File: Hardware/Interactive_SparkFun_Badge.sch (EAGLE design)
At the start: 31 parts, among them J1 AVR_SPI_PRG_6NS, U1 ATMEGA328P, Y1 8MHZ

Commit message: New board design
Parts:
- removed STANDOFF1: STAND-OFF, SparkFun-Electromechanical:STAND-OFF
- removed U$2: FLAME, Local Library:FLAME
- LOGO1: value OSHW-LOGOM -> OSHW-LOGOL; device SparkFun-Aesthetics:OSHW-LOGOM -> SparkFun-Aesthetics:OSHW-LOGOL
- LOGO2: value SFE_LOGO_NAME.1_INCH -> SFE_LOGO_NAME_FLAME.3_INCH; device SparkFun-Aesthetics:SFE_LOGO_NAME.1_INCH -> SparkFun-Aesthetics:SFE_LOGO_NAME_FLAME.3_INCH
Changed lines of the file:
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@@
 <grid distance="0.1" unitdist="inch" unit="inch" style="lines" multiple="1" display="no" altdistance="0.01" altunitdist="inch" altunit="inch"/>
 <layers>
-<layer number="1" name="Top" color="4" fill="1" visible="yes" active="no"/>
-<layer number="2" name="Route2" color="1" fill="3" visible="yes" active="no"/>
-<layer number="3" name="Route3" color="4" fill="3" visible="yes" active="no"/>
-<layer number="4" name="Route4" color="1" fill="4" visible="yes" active="no"/>
-<layer number="5" name="Route5" color="4" fill="4" visible="yes" active="no"/>
-<layer number="6" name="Route6" color="1" fill="8" visible="yes" active="no"/>
-<layer number="7" name="Route7" color="4" fill="8" visible="yes" active="no"/>
-<layer number="8" name="Route8" color="1" fill="2" visible="yes" active="no"/>
-<layer number="9" name="Route9" color="4" fill="2" visible="yes" active="no"/>
-<layer number="10" name="Route10" color="1" fill="7" visible="yes" active="no"/>
-<layer number="11" name="Route11" color="4" fill="7" visible="yes" active="no"/>
-<layer number="12" name="Route12" color="1" fill="5" visible="yes" active="no"/>
-<layer number="13" name="Route13" color="4" fill="5" visible="yes" active="no"/>
-<layer number="14" name="Route14" color="1" fill="6" visible="yes" active="no"/>
-<layer number="15" name="Route15" color="4" fill="6" visible="yes" active="no"/>
-<layer number="16" name="Bottom" color="1" fill="1" visible="yes" active="no"/>
-<layer number="17" name="Pads" color="2" fill="1" visible="yes" active="no"/>
-<layer number="18" name="Vias" color="2" fill="1" visible="yes" active="no"/>
-<layer number="19" name="Unrouted" color="6" fill="1" visible="yes" active="no"/>
-<layer number="20" name="Dimension" color="15" fill="1" visible="yes" active="no"/>
-<layer number="21" name="tPlace" color="16" fill="1" visible="yes" active="no"/>
-<layer number="22" name="bPlace" color="14" fill="1" visible="yes" active="no"/>
-<layer number="23" name="tOrigins" color="15" fill="1" visible="yes" active="no"/>
-<layer number="24" name="bOrigins" color="15" fill="1" visible="yes" active="no"/>
-<layer number="25" name="tNames" color="7" fill="1" visible="yes" active="no"/>
-<layer number="26" name="bNames" color="7" fill="1" visible="yes" active="no"/>
-<layer number="27" name="tValues" color="7" fill="1" visible="yes" active="no"/>
-<layer number="28" name="bValues" color="7" fill="1" visible="yes" active="no"/>
+<layer number="1" name="Top" color="4" fill="1" visible="no" active="no"/>
+<layer number="2" name="Route2" color="1" fill="3" visible="no" active="no"/>
+<layer number="3" name="Route3" color="4" fill="3" visible="no" active="no"/>
+<layer number="4" name="Route4" color="1" fill="4" visible="no" active="no"/>
+<layer number="5" name="Route5" color="4" fill="4" visible="no" active="no"/>
+<layer number="6" name="Route6" color="1" fill="8" visible="no" active="no"/>
+<layer number="7" name="Route7" color="4" fill="8" visible="no" active="no"/>
+<layer number="8" name="Route8" color="1" fill="2" visible="no" active="no"/>
+<layer number="9" name="Route9" color="4" fill="2" visible="no" active="no"/>
+<layer number="10" name="Route10" color="1" fill="7" visible="no" active="no"/>
+<layer number="11" name="Route11" color="4" fill="7" visible="no" active="no"/>
+<layer number="12" name="Route12" color="1" fill="5" visible="no" active="no"/>
+<layer number="13" name="Route13" color="4" fill="5" visible="no" active="no"/>
+<layer number="14" name="Route14" color="1" fill="6" visible="no" active="no"/>
+<layer number="15" name="Route15" color="4" fill="6" visible="no" active="no"/>
+<layer number="16" name="Bottom" color="1" fill="1" visible="no" active="no"/>
+<layer number="17" name="Pads" color="2" fill="1" visible="no" active="no"/>
+<layer number="18" name="Vias" color="2" fill="1" visible="no" active="no"/>
+<layer number="19" name="Unrouted" color="6" fill="1" visible="no" active="no"/>
+<layer number="20" name="Dimension" color="15" fill="1" visible="no" active="no"/>
+<layer number="21" name="tPlace" color="16" fill="1" visible="no" active="no"/>
+<layer number="22" name="bPlace" color="14" fill="1" visible="no" active="no"/>
+<layer number="23" name="tOrigins" color="15" fill="1" visible="no" active="no"/>
+<layer number="24" name="bOrigins" color="15" fill="1" visible="no" active="no"/>
+<layer number="25" name="tNames" color="7" fill="1" visible="no" active="no"/>
+<layer number="26" name="bNames" color="7" fill="1" visible="no" active="no"/>
+<layer number="27" name="tValues" color="7" fill="1" visible="no" active="no"/>
+<layer number="28" name="bValues" color="7" fill="1" visible="no" active="no"/>
 <layer number="29" name="tStop" color="7" fill="3" visible="no" active="no"/>
 <layer number="30" name="bStop" color="7" fill="6" visible="no" active="no"/>
@@
 <layer number="35" name="tGlue" color="7" fill="4" visible="no" active="no"/>
 <layer number="36" name="bGlue" color="7" fill="5" visible="no" active="no"/>
-<layer number="37" name="tTest" color="7" fill="1" visible="yes" active="no"/>
-<layer number="38" name="bTest" color="7" fill="1" visible="yes" active="no"/>
+<layer number="37" name="tTest" color="7" fill="1" visible="no" active="no"/>
+<layer number="38" name="bTest" color="7" fill="1" visible="no" active="no"/>
 <layer number="39" name="tKeepout" color="4" fill="11" visible="no" active="no"/>
 <layer number="40" name="bKeepout" color="1" fill="11" visible="no" active="no"/>
@@
 <layer number="44" name="Drills" color="7" fill="1" visible="no" active="no"/>
 <layer number="45" name="Holes" color="7" fill="1" visible="no" active="no"/>
-<layer number="46" name="Milling" color="3" fill="1" visible="yes" active="no"/>
-<layer number="47" name="Measures" color="7" fill="1" visible="yes" active="no"/>
-<layer number="48" name="Document" color="7" fill="1" visible="yes" active="no"/>
-<layer number="49" name="Reference" color="7" fill="1" visible="yes" active="no"/>
-<layer number="50" name="dxf" color="7" fill="1" visible="yes" active="no"/>
-<layer number="51" name="tDocu" color="6" fill="1" visible="yes" active="no"/>
-<layer number="52" name="bDocu" color="7" fill="1" visible="yes" active="no"/>
-<layer number="53" name="tGND_GNDA" color="7" fill="9" visible="yes" active="no"/>
-<layer number="54" name="bGND_GNDA" color="1" fill="9" visible="yes" active="no"/>
-<layer number="56" name="wert" color="7" fill="1" visible="yes" active="no"/>
-<layer number="57" name="tCAD" color="7" fill="1" visible="yes" active="no"/>
+<layer number="46" name="Milling" color="3" fill="1" visible="no" active="no"/>
+<layer number="47" name="Measures" color="7" fill="1" visible="no" active="no"/>
+<layer number="48" name="Document" color="7" fill="1" visible="no" active="no"/>
+<layer number="49" name="Reference" color="7" fill="1" visible="no" active="no"/>
+<layer number="50" name="dxf" color="7" fill="1" visible="no" active="no"/>
+<layer number="51" name="tDocu" color="6" fill="1" visible="no" active="no"/>
+<layer number="52" name="bDocu" color="7" fill="1" visible="no" active="no"/>
+<layer number="53" name="tGND_GNDA" color="7" fill="9" visible="no" active="no"/>
+<layer number="54" name="bGND_GNDA" color="1" fill="9" visible="no" active="no"/>
+<layer number="56" name="wert" color="7" fill="1" visible="no" active="no"/>
+<layer number="57" name="tCAD" color="7" fill="1" visible="no" active="no"/>
 <layer number="91" name="Nets" color="2" fill="1" visible="yes" active="yes"/>
 <layer number="92" name="Busses" color="1" fill="1" visible="yes" active="yes"/>
@@
 <parts>
 <part name="FRAME1" library="SparkFun-Aesthetics" deviceset="FRAME-LETTER" device=""/>
-<part name="LOGO1" library="SparkFun-Aesthetics" deviceset="OSHW-LOGO" device="M" value="OSHW-LOGOM"/>
-<part name="LOGO2" library="SparkFun-Aesthetics" deviceset="SFE_LOGO_NAME" device=".1_INCH" value="SFE_LOGO_NAME.1_INCH"/>
+<part name="LOGO1" library="SparkFun-Aesthetics" deviceset="OSHW-LOGO" device="L" value="OSHW-LOGOL"/>
+<part name="LOGO2" library="SparkFun-Aesthetics" deviceset="SFE_LOGO_NAME_FLAME" device=".3_INCH" value="SFE_LOGO_NAME_FLAME.3_INCH"/>
 <part name="U1" library="SparkFun-DigitalIC" deviceset="ATMEGA328_SMT" device="" value="ATMEGA328P"/>
 <part name="SG1" library="SparkFun-Electromechanical" deviceset="BUZZER" device="SMD2"/>
@@
 <part name="D2" library="SparkFun-LED" deviceset="LED-GREEN" device="0603" value="GREEN"/>
 <part name="R6" library="SparkFun-Resistors" deviceset="330OHM1/10W1%(0603)" device="" value="330"/>
-<part name="U$2" library="Local Library" deviceset="FLAME" device=""/>
 <part name="JP2" library="SparkFun-Connectors" deviceset="M08" device="1X08"/>
 <part name="JP3" library="SparkFun-Connectors" deviceset="M06" device="LOCK"/>
-<part name="STANDOFF1" library="SparkFun-Electromechanical" deviceset="STAND-OFF" device=""/>
 <part name="FID1" library="SparkFun-Aesthetics" deviceset="FIDUCIAL" device="1X2"/>
 <part name="FID2" library="SparkFun-Aesthetics" deviceset="FIDUCIAL" device="1X2"/>
@@
 <instance part="D2" gate="G$1" x="215.9" y="81.28"/>
 <instance part="R6" gate="G$1" x="215.9" y="91.44" rot="R90"/>
-<instance part="U$2" gate="G$1" x="233.68" y="22.86"/>
 <instance part="JP2" gate="G$1" x="12.7" y="43.18"/>
 <instance part="JP3" gate="G$1" x="43.18" y="45.72"/>
-<instance part="STANDOFF1" gate="G$1" x="246.38" y="27.94"/>
 <instance part="FID1" gate="G$1" x="246.38" y="17.78"/>
 <instance part="FID2" gate="G$1" x="243.84" y="17.78"/>

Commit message: Updating with engineering review changes
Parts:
- removed C1, C2: 10uF, SparkFun-Capacitors:10UF-16V-10%(TANT)
- removed C3: 0.1uF, SparkFun-Capacitors:0.1UF-25V(+80/-20%)(0603)
- removed U3: (no value), SparkFun-PowerIC:MIC52053.3V
- added D3, D4: MBRA140, SparkFun-DiscreteSemi:MBRA140
- JP3: device SparkFun-Connectors:M06LOCK -> SparkFun-Connectors:M06SIP
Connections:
- removed net RAW: BAT1.+, C1.+, U3.EN, U3.IN
- new net 3.3V: D3.A, JP1.4
- new net N$10: BAT1.+, D4.A
- net GND: no longer C1.-, C2.-, C3.2, U3.GND
- net VCC: now also D3.C, D4.C; no longer C2.+, C3.1, JP1.4, U3.OUT
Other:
- note removed: "3.3V Voltage Regulator"
- moved on the sheet: JP3

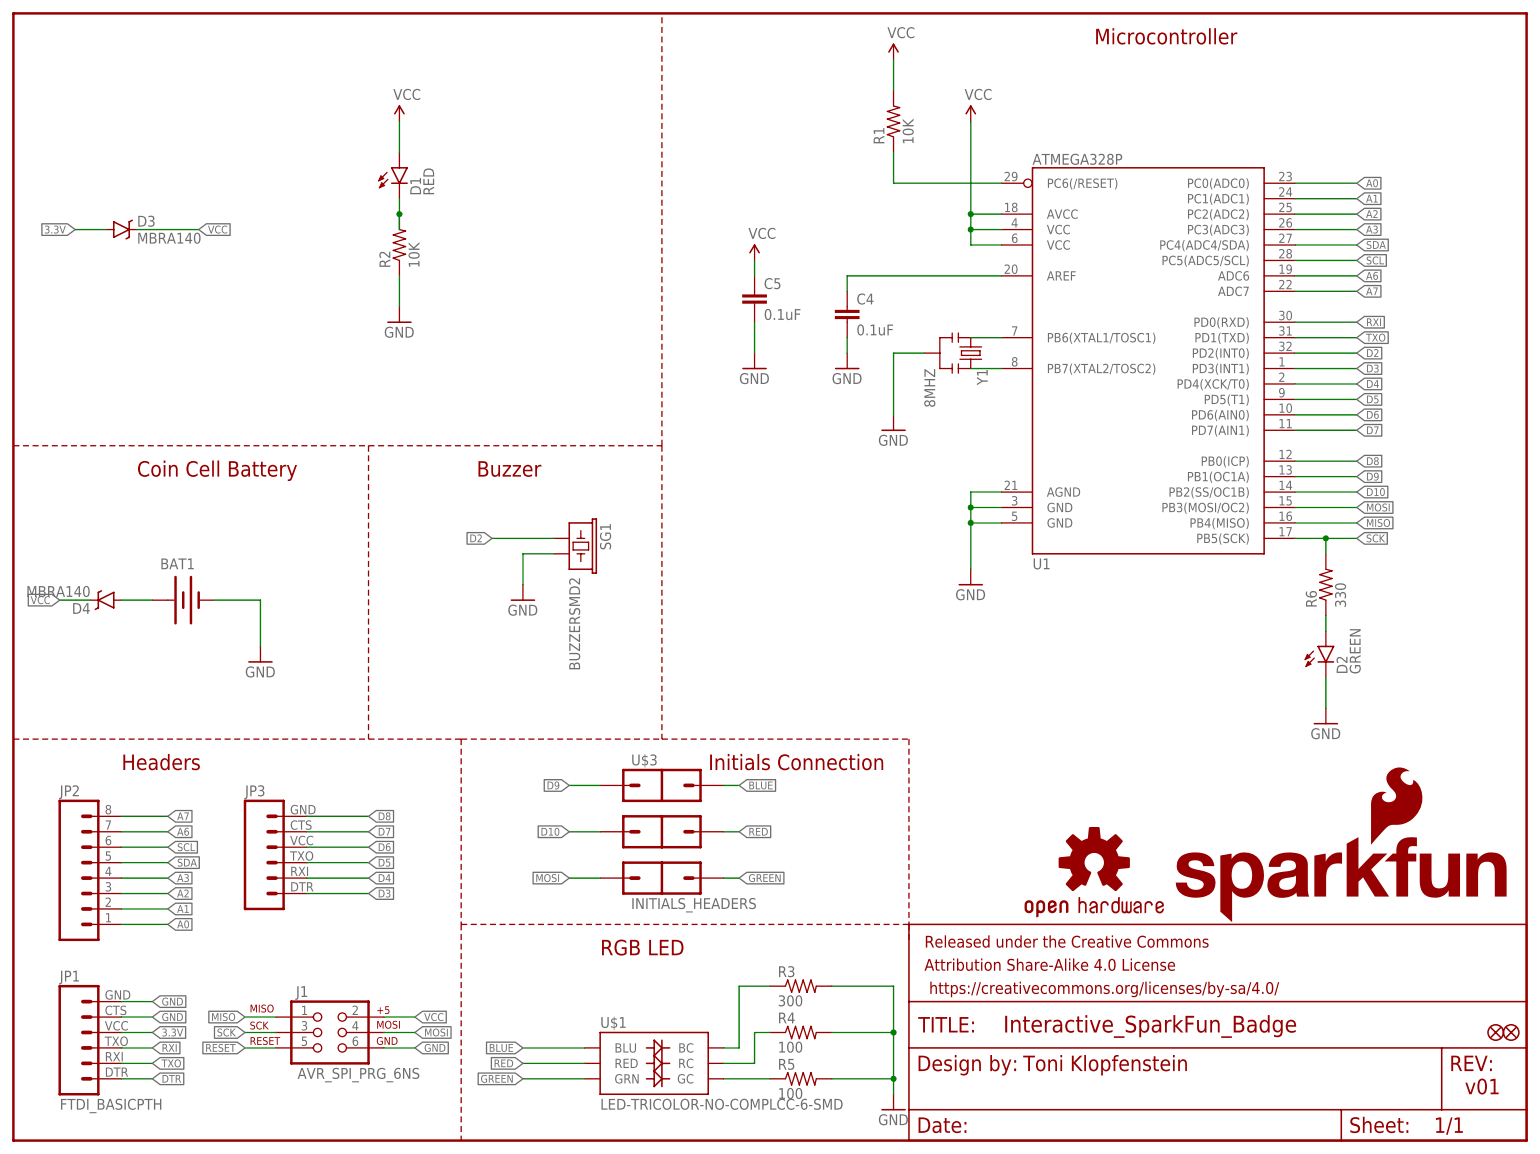
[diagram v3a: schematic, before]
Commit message: Updating to round corners, zener diodes, larger letter boards
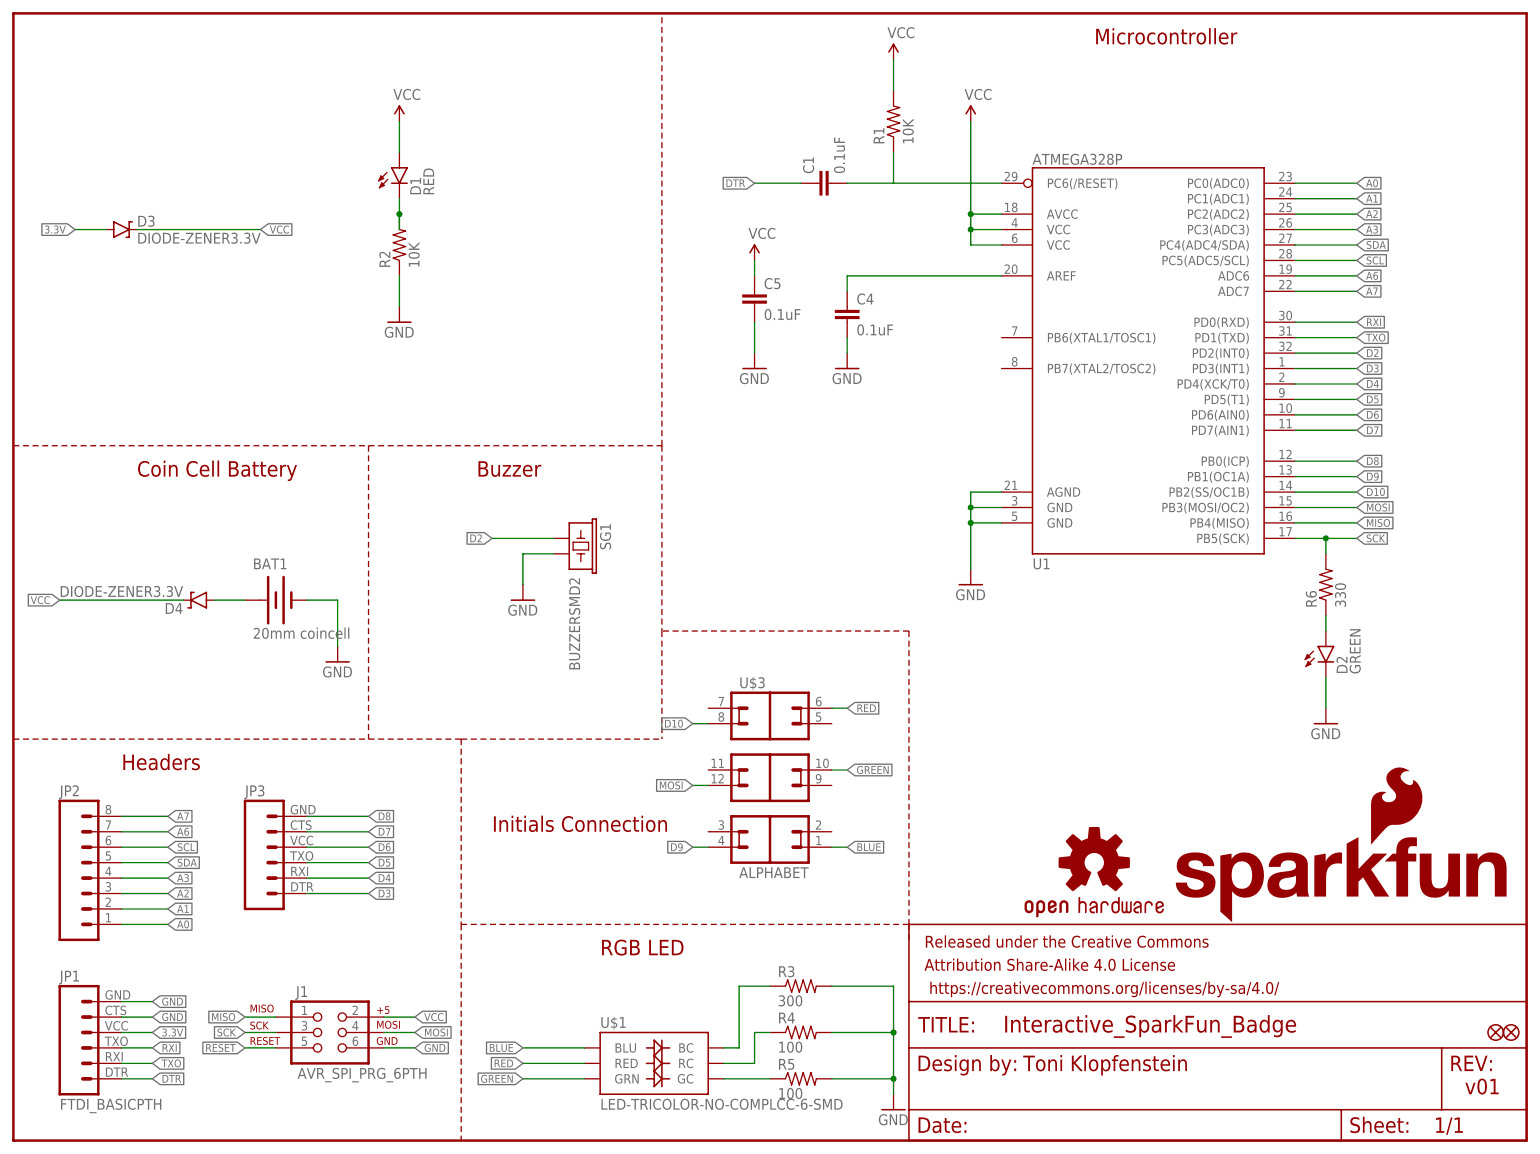
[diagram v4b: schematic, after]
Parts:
- removed Y1: 8MHZ, SparkFun-FreqCtrl:RESONATOR8MHZ
- added C1: 0.1uF, SparkFun-Capacitors:0.1UF-25V(+80/-20%)(0603)
- BAT1: value (none) -> 20mm coincell; device SparkFun-Electromechanical:BATTERY20SMD -> SparkFun-Electromechanical:BATTERY20MM_4LEGS
- D3, D4: value MBRA140 -> DIODE-ZENER3.3V; device SparkFun-DiscreteSemi:MBRA140 -> SparkFun-DiscreteSemi:DIODE-ZENER3.3V
- J1: value AVR_SPI_PRG_6NS -> AVR_SPI_PRG_6PTH; device SparkFun-Connectors:AVR_SPI_PRG_6NS -> SparkFun-Connectors:AVR_SPI_PRG_6PTH
- LOGO1: value OSHW-LOGOL -> OSHW-LOGOM; device SparkFun-Aesthetics:OSHW-LOGOL -> SparkFun-Aesthetics:OSHW-LOGOM
- U$3: value INITIALS_HEADERS -> ALPHABET; device Local Library:INITIALS_HEADERS -> ML8511:ALPHABET
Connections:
- removed net N$2: U1.PB6(XTAL1/TOSC1), Y1.1
- removed net N$3: U1.PB7(XTAL2/TOSC2), Y1.3
- net D10: now also U$3.8; no longer U$3.4
- net D9: now also U$3.4; no longer U$3.2
- net DTR: now also C1.1
- net GND: no longer Y1.2
- net GREEN: now also U$3.10; no longer U$3.5
- net MOSI: now also U$3.12; no longer U$3.6
- net RED: now also U$3.6; no longer U$3.3
- net RESET: now also C1.2
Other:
- moved on the sheet: BAT1, D4
